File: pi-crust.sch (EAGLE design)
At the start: 10 parts

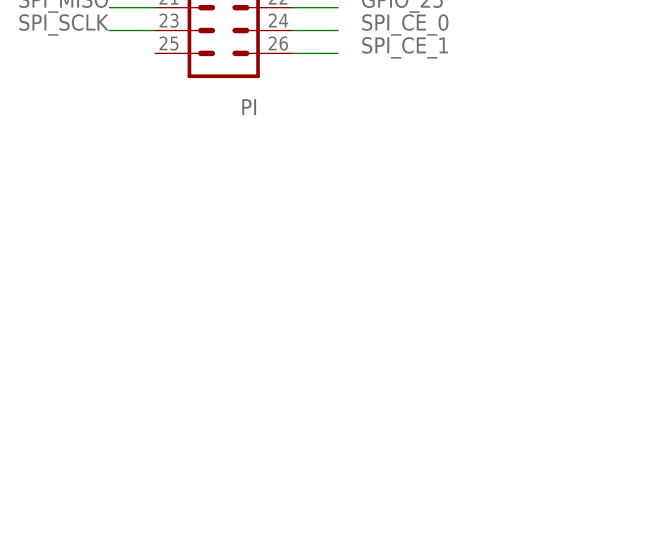
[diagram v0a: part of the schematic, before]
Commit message: v3 board. With Hirose 26 pin connector.
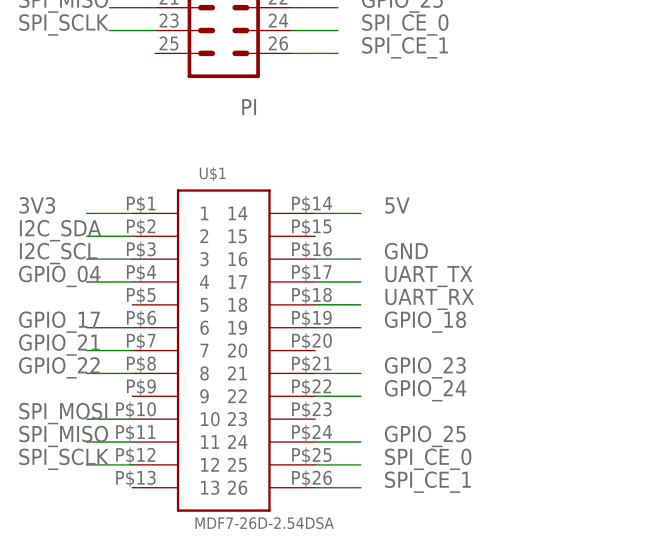
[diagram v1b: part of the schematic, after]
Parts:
- added U$1: MDF7-26D-2.54DSA, E-test-solutions (5):MDF7-26D-2.54DSA
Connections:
- net 3V3: now also U$1.1
- net 5V: now also U$1.14
- net GND: now also U$1.16
- net GPIO_04: now also U$1.4
- net GPIO_17: now also U$1.6
- net GPIO_18: now also U$1.19
- net GPIO_21: now also U$1.7
- net GPIO_22: now also U$1.8
- net GPIO_23: now also U$1.21
- net GPIO_24: now also U$1.22
- net GPIO_25: now also U$1.24
- net I2C_SCL: now also U$1.3
- net I2C_SDA: now also U$1.2
- net SPI_CE_0: now also U$1.25
- net SPI_CE_1: now also U$1.26
- net SPI_MISO: now also U$1.11
- net SPI_MOSI: now also U$1.10
- net SPI_SCLK: now also U$1.12
- net UART_RX: now also U$1.18
- net UART_TX: now also U$1.17
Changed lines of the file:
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@@
 <layer number="121" name="_tsilk" color="7" fill="1" visible="yes" active="yes"/>
 <layer number="122" name="_bsilk" color="7" fill="1" visible="yes" active="yes"/>
+<layer number="125" name="_tNames" color="7" fill="1" visible="no" active="yes"/>
+<layer number="144" name="Drill_legend" color="7" fill="1" visible="no" active="yes"/>
 <layer number="151" name="HeatSink" color="7" fill="1" visible="yes" active="yes"/>
 <layer number="200" name="200bmp" color="1" fill="10" visible="yes" active="yes"/>
@@
 <layer number="207" name="207bmp" color="8" fill="10" visible="yes" active="yes"/>
 <layer number="208" name="208bmp" color="9" fill="10" visible="yes" active="yes"/>
+<layer number="209" name="209bmp" color="7" fill="1" visible="no" active="yes"/>
+<layer number="210" name="210bmp" color="7" fill="1" visible="no" active="yes"/>
+<layer number="211" name="211bmp" color="7" fill="1" visible="no" active="yes"/>
+<layer number="212" name="212bmp" color="7" fill="1" visible="no" active="yes"/>
+<layer number="213" name="213bmp" color="7" fill="1" visible="no" active="yes"/>
+<layer number="214" name="214bmp" color="7" fill="1" visible="no" active="yes"/>
+<layer number="215" name="215bmp" color="7" fill="1" visible="no" active="yes"/>
+<layer number="216" name="216bmp" color="7" fill="1" visible="no" active="yes"/>
+<layer number="217" name="217bmp" color="18" fill="1" visible="no" active="no"/>
+<layer number="218" name="218bmp" color="19" fill="1" visible="no" active="no"/>
+<layer number="219" name="219bmp" color="20" fill="1" visible="no" active="no"/>
+<layer number="220" name="220bmp" color="21" fill="1" visible="no" active="no"/>
+<layer number="221" name="221bmp" color="22" fill="1" visible="no" active="no"/>
+<layer number="222" name="222bmp" color="23" fill="1" visible="no" active="no"/>
+<layer number="223" name="223bmp" color="24" fill="1" visible="no" active="no"/>
+<layer number="224" name="224bmp" color="25" fill="1" visible="no" active="no"/>
 <layer number="250" name="Descript" color="3" fill="1" visible="no" active="no"/>
 <layer number="251" name="SMDround" color="12" fill="11" visible="no" active="no"/>
@@
 <part name="JP4" library="pinhead" deviceset="PINHD-1X1" device="" value="3V3"/>
 <part name="FRAME1" library="SparkFun" deviceset="FRAME-LETTER" device=""/>
+<part name="U$1" library="E-test-solutions (5)" deviceset="MDF7-26D-2.54DSA" device=""/>
 </parts>
 <sheets>
@@
 <instance part="FRAME1" gate="G$1" x="0" y="0"/>
 <instance part="FRAME1" gate="G$2" x="147.32" y="0"/>
+<instance part="U$1" gate="G$1" x="40.64" y="58.42"/>
 </instances>
 <busses>
@@
 <pinref part="JP1" gate="G$1" pin="7"/>
 </segment>
+<segment>
+<pinref part="U$1" gate="G$1" pin="4"/>
+<wire x1="30.48" y1="66.04" x2="25.4" y2="66.04" width="0.1524" layer="91"/>
+<label x="17.78" y="66.04" size="1.778" layer="95"/>
+</segment>
 </net>
 <net name="GPIO_17" class="0">
@@
 <pinref part="JP1" gate="G$1" pin="11"/>
 </segment>
+<segment>
+<pinref part="U$1" gate="G$1" pin="6"/>
+<wire x1="30.48" y1="60.96" x2="25.4" y2="60.96" width="0.1524" layer="91"/>
+<label x="17.78" y="60.96" size="1.778" layer="95"/>
+</segment>
 </net>
 <net name="GPIO_18" class="0">
@@
 <pinref part="JP1" gate="G$1" pin="12"/>
 </segment>
+<segment>
+<pinref part="U$1" gate="G$1" pin="19"/>
+<wire x1="50.8" y1="60.96" x2="55.88" y2="60.96" width="0.1524" layer="91"/>
+<label x="58.42" y="60.96" size="1.778" layer="95"/>
+</segment>
 </net>
 <net name="GPIO_21" class="0">
@@
 <pinref part="JP1" gate="G$1" pin="13"/>
 </segment>
+<segment>
+<pinref part="U$1" gate="G$1" pin="7"/>
+<wire x1="30.48" y1="58.42" x2="25.4" y2="58.42" width="0.1524" layer="91"/>
+<label x="17.78" y="58.42" size="1.778" layer="95"/>
+</segment>
 </net>
 <net name="GPIO_22" class="0">
@@
 <pinref part="JP1" gate="G$1" pin="15"/>
 </segment>
+<segment>
+<pinref part="U$1" gate="G$1" pin="8"/>
+<wire x1="30.48" y1="55.88" x2="25.4" y2="55.88" width="0.1524" layer="91"/>
+<label x="17.78" y="55.88" size="1.778" layer="95"/>
+</segment>
 </net>
 <net name="GPIO_23" class="0">
@@
 <pinref part="JP1" gate="G$1" pin="16"/>
 </segment>
+<segment>
+<pinref part="U$1" gate="G$1" pin="21"/>
+<wire x1="50.8" y1="55.88" x2="55.88" y2="55.88" width="0.1524" layer="91"/>
+<label x="58.42" y="55.88" size="1.778" layer="95"/>
+</segment>
 </net>
 <net name="GPIO_24" class="0">
@@
 <pinref part="JP1" gate="G$1" pin="18"/>
 </segment>
+<segment>
+<pinref part="U$1" gate="G$1" pin="22"/>
+<wire x1="50.8" y1="53.34" x2="55.88" y2="53.34" width="0.1524" layer="91"/>
+<label x="58.42" y="53.34" size="1.778" layer="95"/>
+</segment>
 </net>
 <net name="GPIO_25" class="0">
@@
 <pinref part="JP1" gate="G$1" pin="22"/>
 </segment>
+<segment>
+<pinref part="U$1" gate="G$1" pin="24"/>
+<wire x1="50.8" y1="48.26" x2="55.88" y2="48.26" width="0.1524" layer="91"/>
+<label x="58.42" y="48.26" size="1.778" layer="95"/>
+</segment>
 </net>
 <net name="GND" class="0">
@@
 <pinref part="JP1" gate="G$1" pin="6"/>
 </segment>
+<segment>
+<pinref part="U$1" gate="G$1" pin="16"/>
+<wire x1="50.8" y1="68.58" x2="55.88" y2="68.58" width="0.1524" layer="91"/>
+<label x="58.42" y="68.58" size="1.778" layer="95"/>
+</segment>
 </net>
 <net name="5V" class="0">
@@
 <pinref part="JP1" gate="G$1" pin="2"/>
 </segment>
+<segment>
+<pinref part="U$1" gate="G$1" pin="14"/>
+<wire x1="50.8" y1="73.66" x2="55.88" y2="73.66" width="0.1524" layer="91"/>
+<label x="58.42" y="73.66" size="1.778" layer="95"/>
+</segment>
 </net>
 <net name="UART_TX" class="0">
@@
 <pinref part="JP1" gate="G$1" pin="8"/>
 </segment>
+<segment>
+<pinref part="U$1" gate="G$1" pin="17"/>
+<wire x1="50.8" y1="66.04" x2="55.88" y2="66.04" width="0.1524" layer="91"/>
+<label x="58.42" y="66.04" size="1.778" layer="95"/>
+</segment>
 </net>
 <net name="UART_RX" class="0">
@@
 <pinref part="JP1" gate="G$1" pin="10"/>
 </segment>
+<segment>
+<pinref part="U$1" gate="G$1" pin="18"/>
+<wire x1="50.8" y1="63.5" x2="55.88" y2="63.5" width="0.1524" layer="91"/>
+<label x="58.42" y="63.5" size="1.778" layer="95"/>
+</segment>
 </net>
 <net name="SPI_CE_1" class="0">
@@
 <pinref part="JP1" gate="G$1" pin="26"/>
 </segment>
+<segment>
+<pinref part="U$1" gate="G$1" pin="26"/>
+<wire x1="50.8" y1="43.18" x2="55.88" y2="43.18" width="0.1524" layer="91"/>
+<label x="58.42" y="43.18" size="1.778" layer="95"/>
+</segment>
 </net>
 <net name="SPI_MOSI" class="0">
@@
 <pinref part="JP1" gate="G$1" pin="19"/>
 </segment>
+<segment>
+<pinref part="U$1" gate="G$1" pin="10"/>
+<wire x1="30.48" y1="50.8" x2="25.4" y2="50.8" width="0.1524" layer="91"/>
+<label x="17.78" y="50.8" size="1.778" layer="95"/>
+</segment>
 </net>
 <net name="SPI_MISO" class="0">
@@
 <pinref part="JP1" gate="G$1" pin="21"/>
 </segment>
+<segment>
+<pinref part="U$1" gate="G$1" pin="11"/>
+<wire x1="30.48" y1="48.26" x2="25.4" y2="48.26" width="0.1524" layer="91"/>
+<label x="17.78" y="48.26" size="1.778" layer="95"/>
+</segment>
 </net>
 <net name="I2C_SDA" class="0">
@@
 <pinref part="JP1" gate="G$1" pin="3"/>
 </segment>
+<segment>
+<pinref part="U$1" gate="G$1" pin="2"/>
+<wire x1="30.48" y1="71.12" x2="25.4" y2="71.12" width="0.1524" layer="91"/>
+<label x="17.78" y="71.12" size="1.778" layer="95"/>
+</segment>
 </net>
 <net name="I2C_SCL" class="0">
@@
 <pinref part="JP1" gate="G$1" pin="5"/>
 </segment>
+<segment>
+<pinref part="U$1" gate="G$1" pin="3"/>
+<wire x1="30.48" y1="68.58" x2="25.4" y2="68.58" width="0.1524" layer="91"/>
+<label x="17.78" y="68.58" size="1.778" layer="95"/>
+</segment>
 </net>
 <net name="SPI_CE_0" class="0">
@@
 <pinref part="JP1" gate="G$1" pin="24"/>
 </segment>
+<segment>
+<pinref part="U$1" gate="G$1" pin="25"/>
+<wire x1="50.8" y1="45.72" x2="55.88" y2="45.72" width="0.1524" layer="91"/>
+<label x="58.42" y="45.72" size="1.778" layer="95"/>
+</segment>
 </net>
 <net name="3V3" class="0">
@@
 <pinref part="JP1" gate="G$1" pin="1"/>
 </segment>
+<segment>
+<pinref part="U$1" gate="G$1" pin="1"/>
+<wire x1="30.48" y1="73.66" x2="25.4" y2="73.66" width="0.1524" layer="91"/>
+<label x="17.78" y="73.66" size="1.778" layer="95"/>
+</segment>
 </net>
 <net name="SPI_SCLK" class="0">
@@
 <pinref part="JP7" gate="A" pin="6"/>
 </segment>
-</net>
+<segment>
+<pinref part="U$1" gate="G$1" pin="12"/>
+<wire x1="30.48" y1="45.72" x2="25.4" y2="45.72" width="0.1524" layer="91"/>
+<label x="17.78" y="45.72" size="1.778" layer="95"/>
+</segment>
+</net>

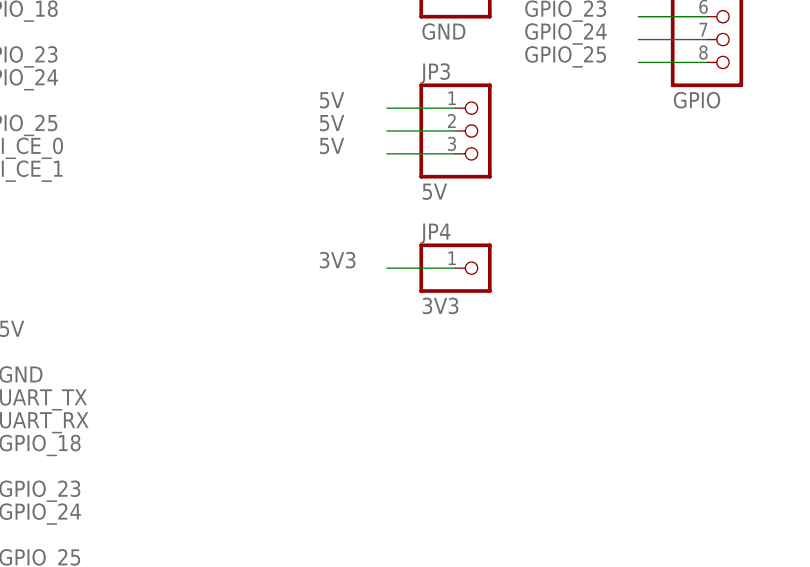
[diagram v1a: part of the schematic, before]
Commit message: V4: Replaced single 3V3 header with a double. Actually makes it cheaper to make and a 2nd connector is always handy. Shuffled the UART along a little.
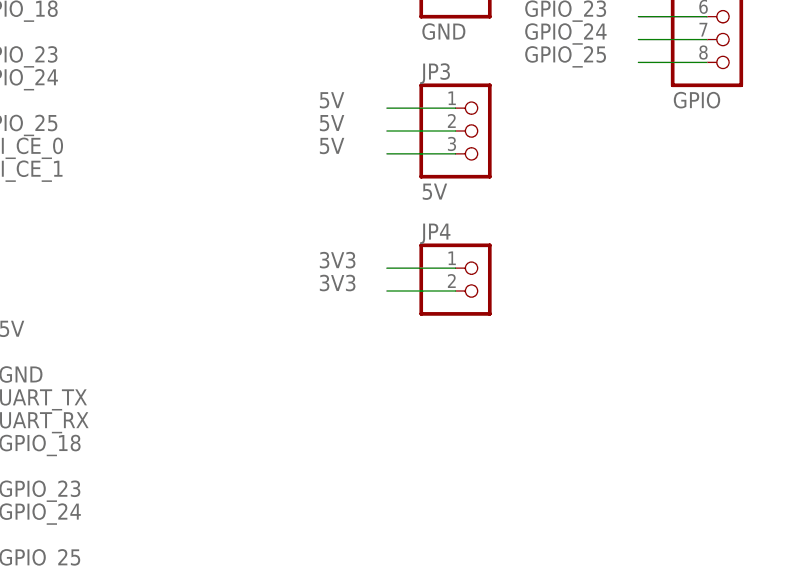
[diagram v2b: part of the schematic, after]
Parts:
- JP4: value 3V3 -> (none); device pinhead:PINHD-1X1 -> pinhead:PINHD-1X2
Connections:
- net 3V3: now also JP4.2
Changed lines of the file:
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@@
 <part name="JP2" library="pinhead" deviceset="PINHD-1X5" device="" value="GND"/>
 <part name="JP3" library="pinhead" deviceset="PINHD-1X3" device="" value="5V"/>
-<part name="JP4" library="pinhead" deviceset="PINHD-1X1" device="" value="3V3"/>
 <part name="FRAME1" library="SparkFun" deviceset="FRAME-LETTER" device=""/>
 <part name="U$1" library="E-test-solutions (5)" deviceset="MDF7-26D-2.54DSA" device=""/>
+<part name="JP4" library="pinhead" deviceset="PINHD-1X2" device=""/>
 </parts>
 <sheets>
@@
 <instance part="JP2" gate="A" x="111.76" y="116.84"/>
 <instance part="JP3" gate="A" x="111.76" y="96.52"/>
-<instance part="JP4" gate="G$1" x="111.76" y="81.28"/>
 <instance part="FRAME1" gate="G$1" x="0" y="0"/>
 <instance part="FRAME1" gate="G$2" x="147.32" y="0"/>
 <instance part="U$1" gate="G$1" x="40.64" y="58.42"/>
+<instance part="JP4" gate="G$1" x="111.76" y="78.74"/>
 </instances>
 <busses>
@@
 <net name="3V3" class="0">
 <segment>
-<wire x1="109.22" y1="81.28" x2="101.6" y2="81.28" width="0.1524" layer="91"/>
-<label x="93.98" y="81.28" size="1.778" layer="95"/>
-<pinref part="JP4" gate="G$1" pin="1"/>
-</segment>
-<segment>
 <wire x1="33.02" y1="121.92" x2="27.94" y2="121.92" width="0.1524" layer="91"/>
 <label x="17.78" y="121.92" size="1.778" layer="95"/>
@@
 <label x="17.78" y="73.66" size="1.778" layer="95"/>
 </segment>
-</net>
+<segment>
+<pinref part="JP4" gate="G$1" pin="2"/>
+<wire x1="109.22" y1="78.74" x2="101.6" y2="78.74" width="0.1524" layer="91"/>
+<label x="93.98" y="78.74" size="1.778" layer="95"/>
+</segment>
+<segment>
+<pinref part="JP4" gate="G$1" pin="1"/>
+<wire x1="109.22" y1="81.28" x2="101.6" y2="81.28" width="0.1524" layer="91"/>
+<label x="93.98" y="81.28" size="1.778" layer="95"/>
+</segment>
+</net>
